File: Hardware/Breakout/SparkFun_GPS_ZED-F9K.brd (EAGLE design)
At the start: 43.2 x 50.8 mm, 148 parts, among them J1 U.FL, J3 QWIIC_RIGHT_ANGLE, J4 QWIIC_RIGHT_ANGLE, U1 UBLOX_ZED_F9R, U2 3.3V, U4 HCPL-270L

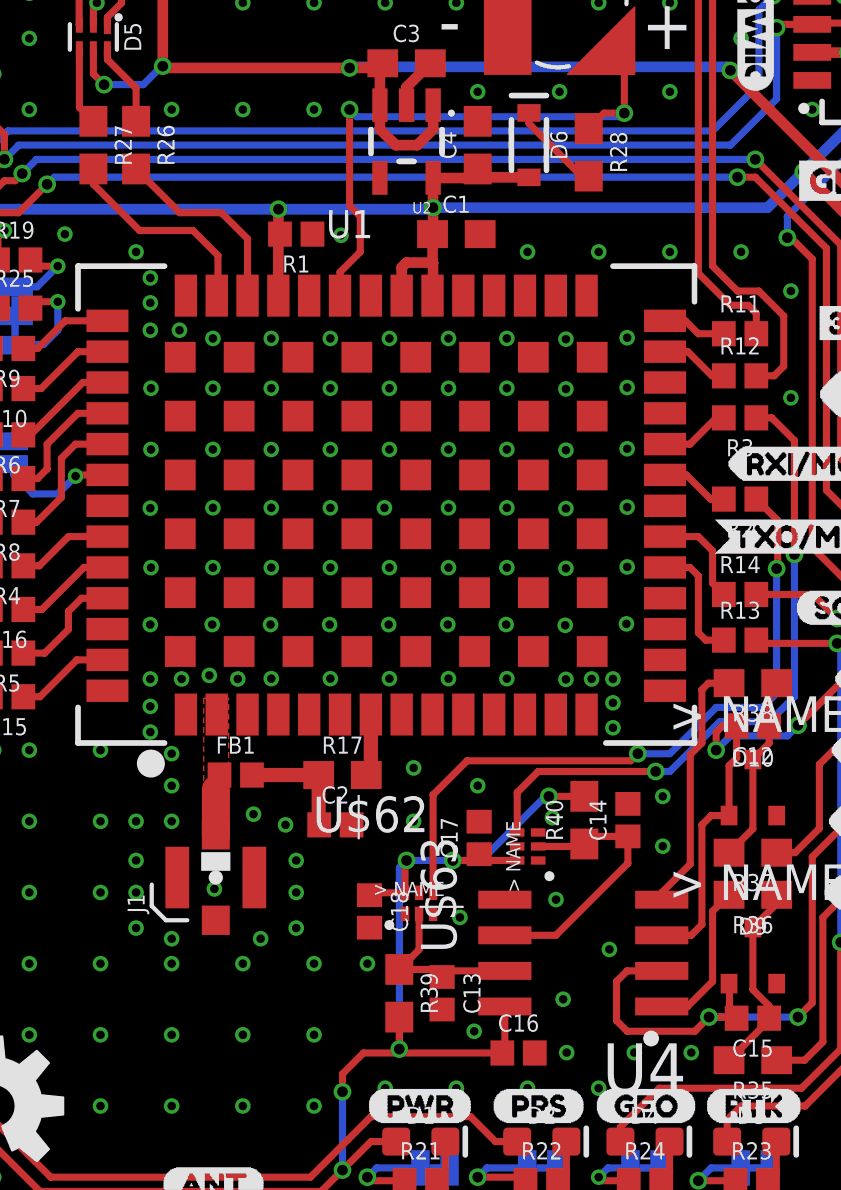
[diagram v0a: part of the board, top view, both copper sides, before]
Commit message: Removes gerbers, removes caps from schmitt trigger on both designs, adds 1uF cap to V_USB on breakout
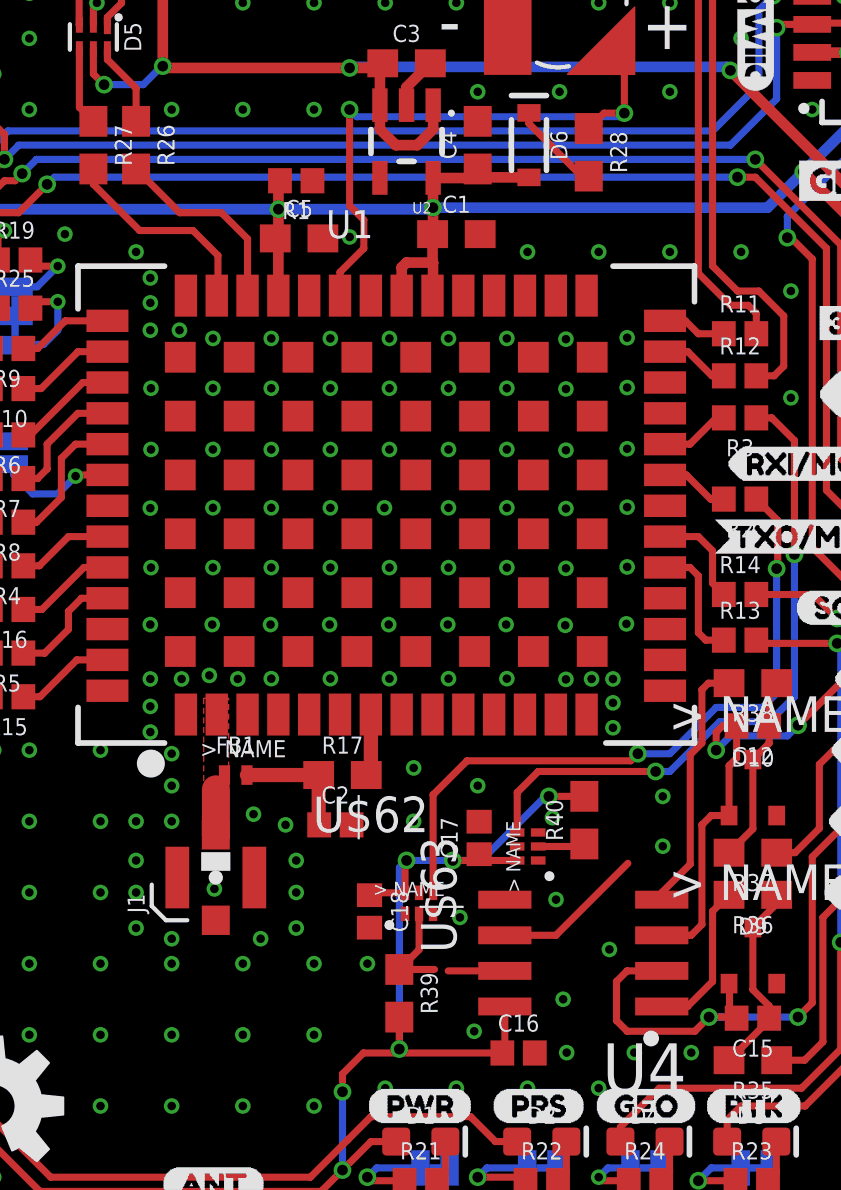
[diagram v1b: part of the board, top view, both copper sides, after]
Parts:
- removed C13, C14: 22nF, SparkFun-Capacitors:0402
- added C5: 1.0uF, SparkFun-Capacitors:0603
- FB1: value FERRITE_BEAD-120_OHM-0402 -> 120NH; device SparkFun-Coils:0402 -> SparkFun-Coils:0402_MURATA
- R17: value 10 -> 33
- moved R1 1.91 mm to (19.7, 36.8)
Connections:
- net 3.3V: now also C5.1
- net DIR_SCHMITT: no longer C14.1
- net GND: now also C5.2; no longer C13.2, C14.2
- net N$5: now also FB1.P2; no longer FB1.2
- net RF_IN: now also FB1.P1; no longer FB1.1
- net WT_SCHMITT: no longer C13.1
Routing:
- net DIR_SCHMITT: track 9.76 -> 7.52 mm
- net 3.3V: track 156.9 -> 158.0 mm
- net WT_SCHMITT: track 6.25 -> 5.56 mm

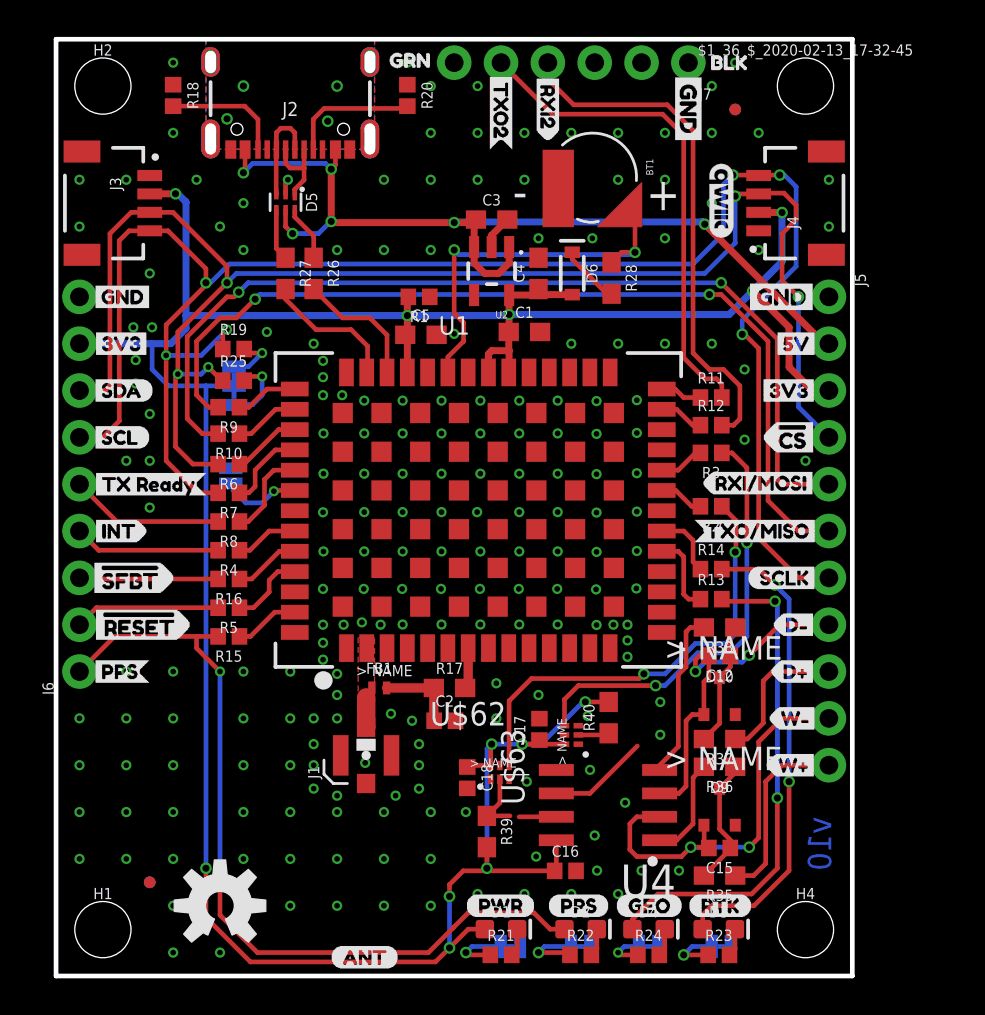
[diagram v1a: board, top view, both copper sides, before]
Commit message: Updates wheel tick and direction circuitry with correct grounding
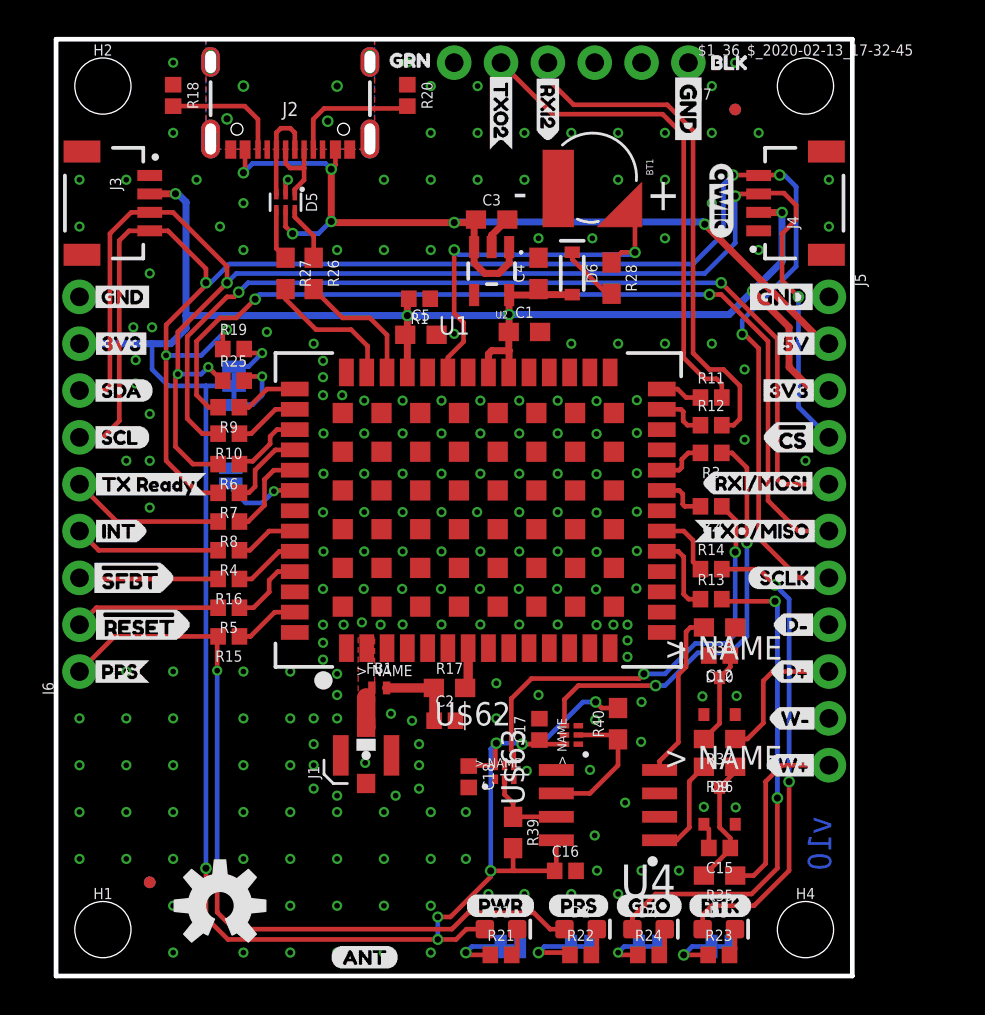
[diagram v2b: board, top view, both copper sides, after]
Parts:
- moved R39 1.42 mm to (24.8, 7.78)
- moved R40 0.61 mm to (30.5, 13.7)
- moved U$62 0.25 mm to (24.3, 11.0)
- moved R1 0.10 mm to (19.7, 36.7)
- moved C18 0.09 mm to (22.4, 10.8)
- moved D9 0.05 mm to (36.0, 9.21)
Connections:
- removed net DIR-: C12.2, D10.P1, J5.8, U4.P3
- removed net WT-: C15.2, D9.P1, J5.10, U4.P2
- net GND: now also C12.2, C15.2, D10.P1, D9.P1, J5.10, J5.8, U4.P2, U4.P3
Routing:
- net WT-: track 22.6 -> 0.00 mm, vias 2 -> 0
- net DIR-: track 19.3 -> 0.00 mm, vias 2 -> 0
- net PPS: track 44.7 -> 43.2 mm
- net GND: track 2.69 -> 4.08 mm, vias 203 -> 211
- net WT_SCHMITT: track 5.56 -> 4.59 mm
- net 3.3V: track 158.0 -> 157.0 mm
